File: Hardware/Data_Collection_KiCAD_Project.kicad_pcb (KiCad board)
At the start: 4 copper layers, 80 x 87.2 mm, 77 parts, among them IC1 STM32L562VET6Q, J1 USB_B_Micro, J2 Conn_Coaxial, J3 L717SDC37P1ACH4F, Q1 SI1040X-T1-GE3, U1 LM317T, U2 USBLC6-2SC6, U3 MCP9808_MSOP, U4 MAX-8Q, U6 W25Q32JVSS, U7 MS5607-02BA, U8 BNO055, U9 KX134-1211, Y1 32MHz, Y2 32.768kHz

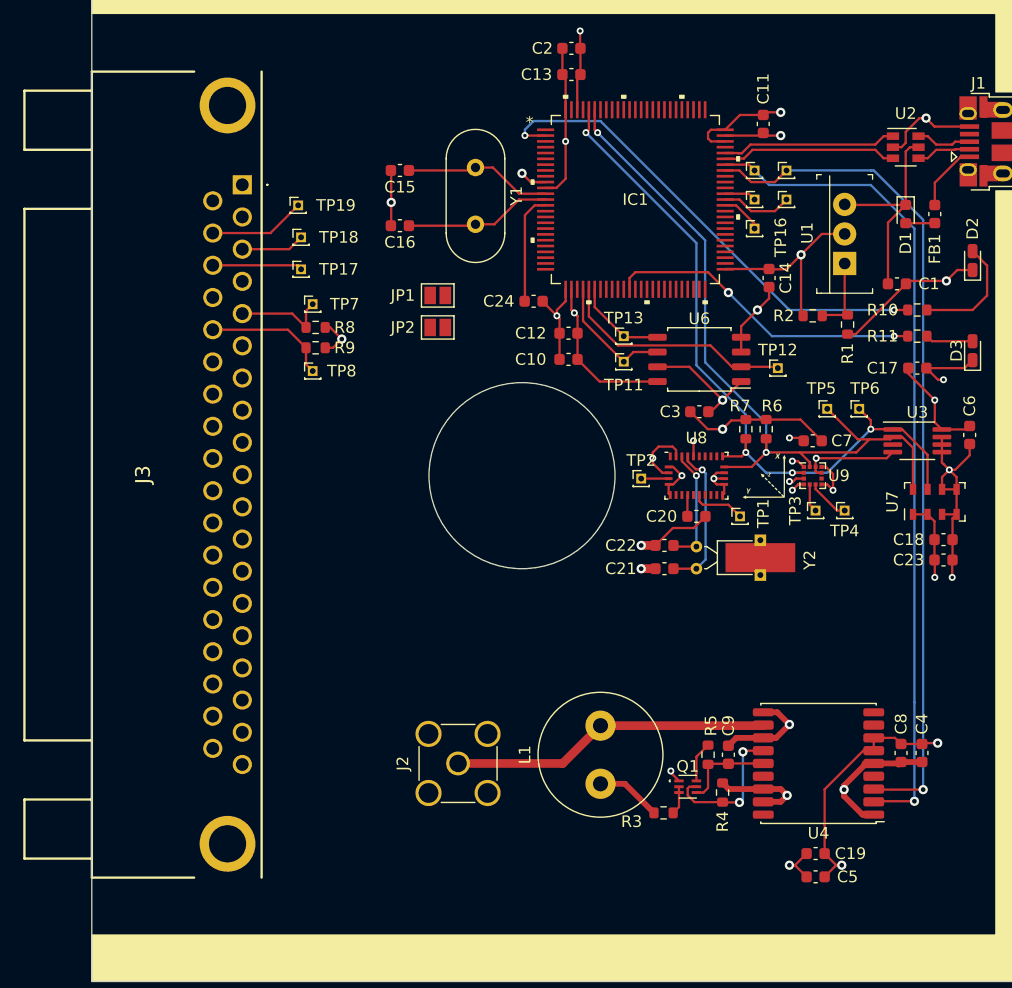
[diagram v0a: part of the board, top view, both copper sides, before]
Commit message: GPS layout change and test point tweaks
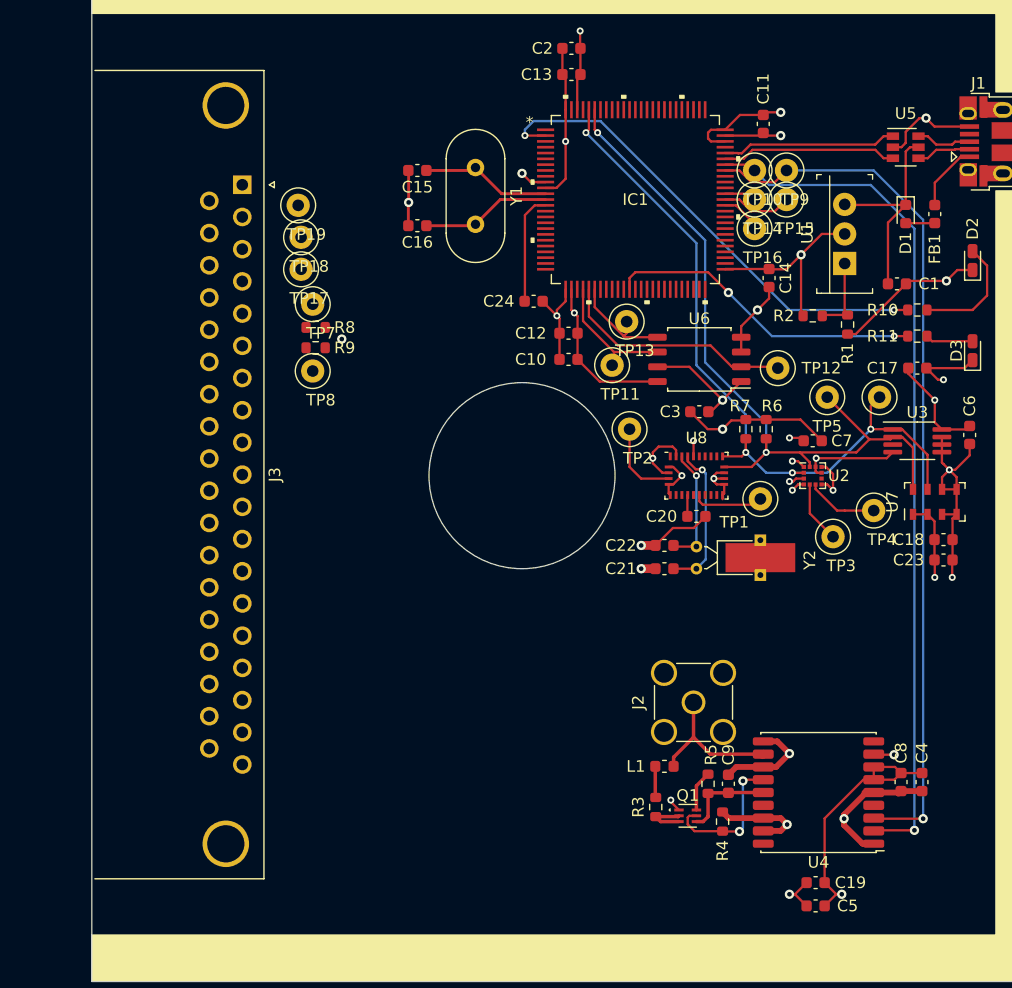
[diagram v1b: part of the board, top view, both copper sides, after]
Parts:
- removed G***: LOGO, XYZ:XYZ_Plane
- removed JP1: VDDA Bridge, Jumper:SolderJumper-2_P1.3mm_Open_Pad1.0x1.5mm
- removed JP2: VDD_SMPS, Jumper:SolderJumper-2_P1.3mm_Open_Pad1.0x1.5mm
- J3: footprint L717SDC37P1ACH4F:L717SDC37P1ACH4F -> Connector_Dsub:DSUB-37_Male_Horizontal_P2.77x2.84mm_EdgePinOffset9.90mm_Housed_MountingHolesOffset11.32mm
- L1: footprint Inductor_THT:L_Radial_D10.5mm_P5.00mm_Abacron_AISR-01 -> Inductor_SMD:L_0603_1608Metric
- TP1, TP10, TP11, TP12, TP13, TP14, TP15, TP16, TP17, TP18, TP19, TP2, TP3, TP4, TP5, TP6, TP7, TP8, TP9: footprint Connector_PinHeader_1.00mm:PinHeader_1x01_P1.00mm_Vertical -> TestPoint:TestPoint_Loop_D1.80mm_Drill1.0mm_Beaded
- moved J2 20.9 mm to (131.8, 121.0)
- moved L1 5.70 mm to (129.2, 126.5), turned to 0 degrees
- moved TP2 4.37 mm to (126.2, 97.5)
- moved TP3 2.70 mm to (143.8, 106.7)
- moved C19 2.50 mm to (142.2, 136.5)
- moved C4 2.50 mm to (151.4, 127.8)
- moved C5 2.50 mm to (142.2, 138.5)
- moved C8 2.50 mm to (149.6, 127.8)
- moved C9 2.50 mm to (134.8, 128.0)
- moved Q1 2.50 mm to (131.2, 130.7)
- moved R4 2.50 mm to (134.2, 131.2)
- moved R5 2.50 mm to (133.0, 128.0)
- moved TP4 2.50 mm to (147.2, 104.5)
- moved U4 2.50 mm to (142.5, 128.7)
- moved TP1 2.30 mm to (137.5, 103.5)
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- renumbered U9 to U2, U2 to U5
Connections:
- net /Main Bus/Fire renamed /37 Pin DSUB Bus/Fire
- net /Main Bus/Fire_redundant renamed /37 Pin DSUB Bus/Fire_redundant
- IC1 pad 21: Net-(IC1-Pad21) -> +3V3
- IC1 pad 46: Net-(IC1-Pad46) -> +3V3
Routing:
- net /MAX-8Q/GPS_ANT_NET: track 27.6 -> 12.9 mm
- net /EXT_SDA: track 10.9 -> 0.81 mm
- net /SPI2_MOSI: track 8.33 -> 0.00 mm
- net /EXT_SCL: track 8.21 -> 0.81 mm
- net /SPI2_SCK: track 7.74 -> 0.49 mm
- net /SPI2_MISO: track 5.48 -> 0.00 mm
- net /BNO055/~BNO055_BTL: track 2.36 -> 7.03 mm
- net Net-(L1-Pad1): track 6.56 -> 2.69 mm
- net /KX134-1211/KX134_INT1: track 2.44 -> 5.32 mm
- net /USART1_TX: track 72.9 -> 75.4 mm
- net /USART1_RX: track 71.3 -> 73.8 mm
- net /KX134-1211/KX134_INT2: track 3.65 -> 6.15 mm
- net Net-(Q1-Pad2): track 2.46 -> 4.21 mm
- net /BNO055/~BNO055_RESET: track 4.58 -> 6.12 mm
- net Net-(C15-Pad1): track 12.8 -> 11.3 mm
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
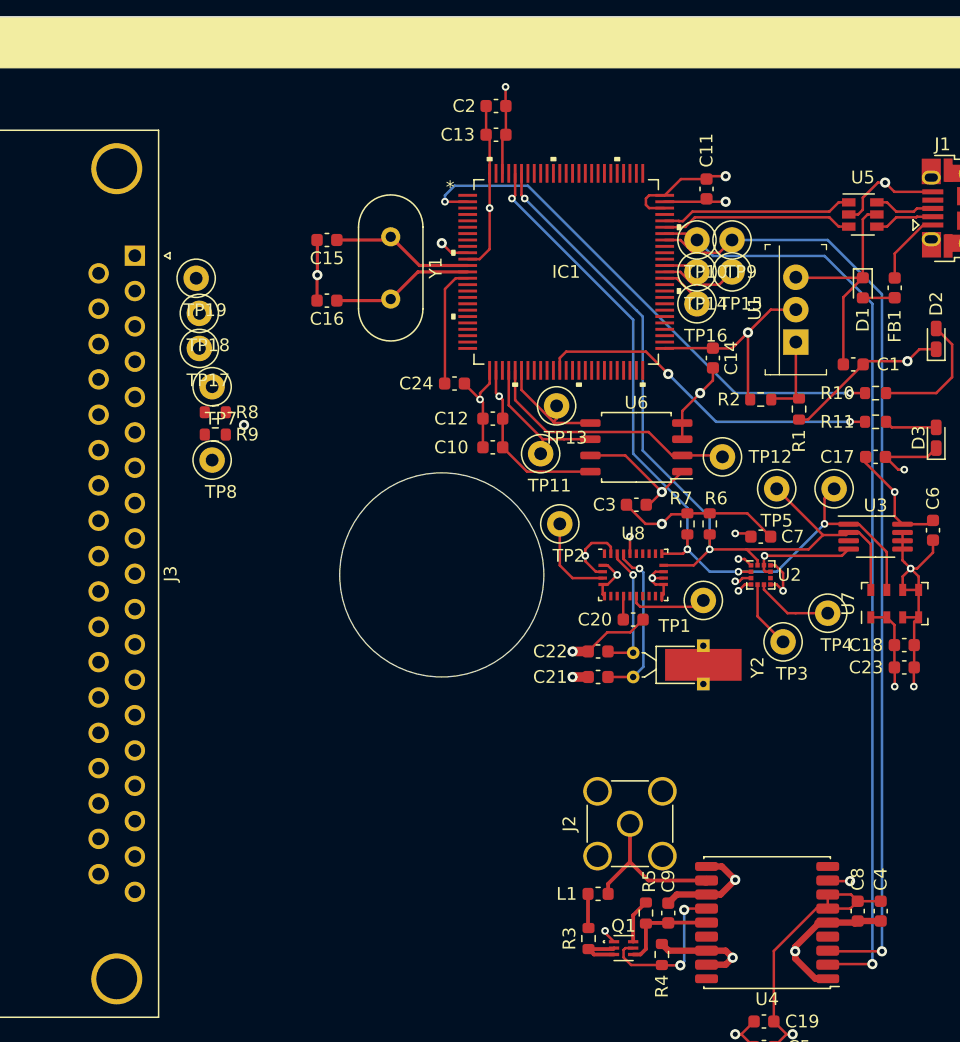
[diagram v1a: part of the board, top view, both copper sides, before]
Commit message: Finalized
Everything is routed. There are probably some things that need rerouting or adjustment.
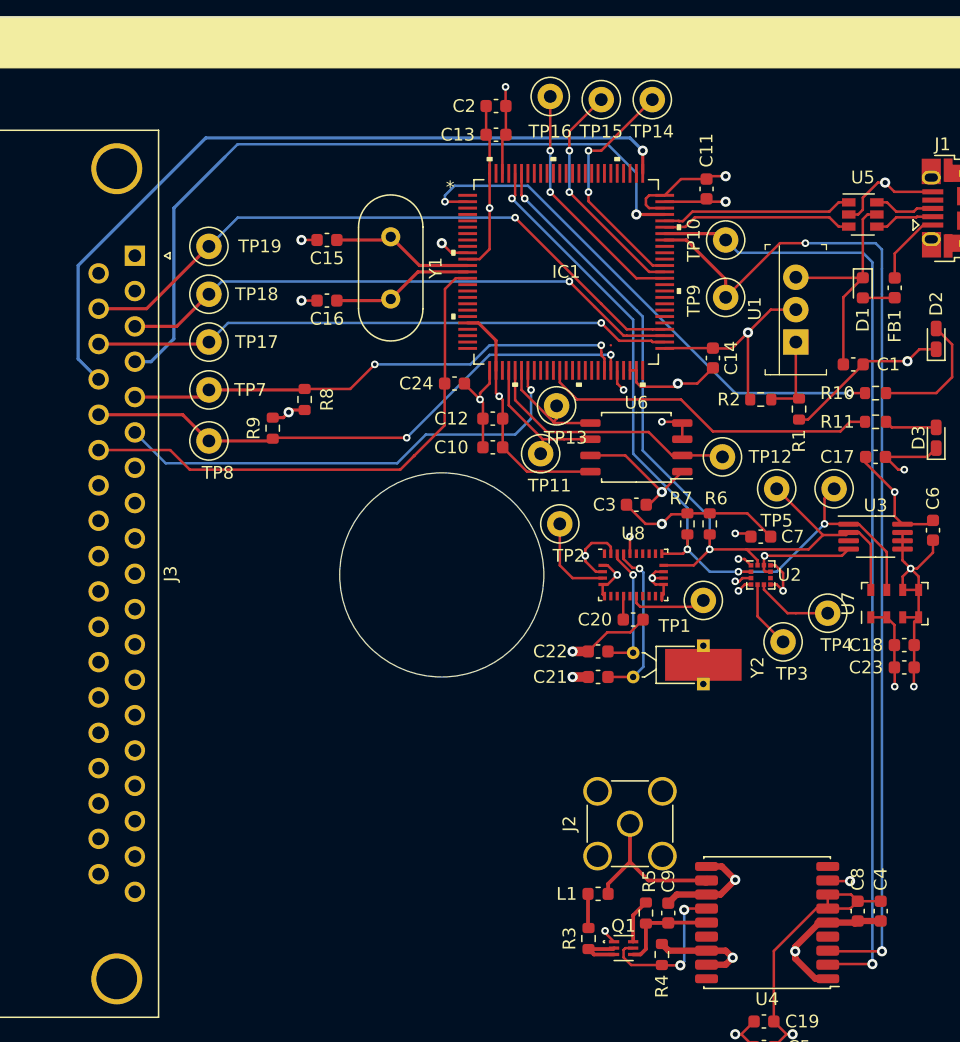
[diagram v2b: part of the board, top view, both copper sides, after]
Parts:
- moved TP16 19.9 mm to (125.5, 64.0)
- moved TP15 17.0 mm to (129.5, 64.2)
- moved TP14 13.9 mm to (133.5, 64.2)
- moved R8 7.07 mm to (106.2, 87.7), turned to 270 degrees
- moved R9 4.53 mm to (103.8, 90.0), turned to 90 degrees
- moved TP9 4.53 mm to (139.2, 79.7)
- moved TP19 2.69 mm to (98.8, 75.7)
- moved TP10 2.25 mm to (139.2, 75.2)
- moved TP18 1.68 mm to (98.8, 79.5)
- moved TP8 1.52 mm to (98.8, 91.0)
- moved TP17 0.90 mm to (98.8, 83.2)
- moved TP7 0.35 mm to (98.8, 87.0)
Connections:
- J3 pad 20: +5V -> Net-(J3-Pad20)
- J3 pad 37: +5V -> Net-(J3-Pad37)
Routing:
- net /SWCLK: track 0.00 -> 60.2 mm, vias 0 -> 1
- net /SWDIO: track 0.00 -> 58.8 mm, vias 0 -> 1
- net /SPI2_MOSI: track 0.00 -> 50.9 mm, vias 0 -> 1
- net /SPI2_MISO: track 0.00 -> 45.5 mm, vias 0 -> 1
- net /SPI2_SCK: track 0.49 -> 45.7 mm, vias 0 -> 1
- net /EXT_SDA: track 0.81 -> 45.0 mm, vias 0 -> 2
- net /EXT_SCL: track 0.81 -> 40.3 mm, vias 0 -> 2
- net /I2C_ALERT: track 0.00 -> 37.4 mm, vias 0 -> 1
- net /NRST: track 9.55 -> 42.2 mm
- net Net-(IC1-Pad64): track 2.74 -> 18.7 mm, vias 0 -> 2
- net Net-(IC1-Pad62): track 3.60 -> 19.3 mm, vias 0 -> 2
- net Net-(IC1-Pad63): track 6.11 -> 18.3 mm, vias 0 -> 2
- net +3V3: track 117.6 -> 126.8 mm, vias 13 -> 14
- net /USART1_TX: track 75.4 -> 81.0 mm, vias 1 -> 2
- net GND: track 157.6 -> 159.8 mm, vias 26 -> 28
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
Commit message: Schematic Tweaks and Board Dimensioned
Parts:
- removed TP10, TP11, TP12, TP13, TP17, TP18, TP19, TP5, TP6, TP7, TP8, TP9: Debug Pad, TestPoint:TestPoint_Loop_D1.80mm_Drill1.0mm_Beaded
- added J4: I2C1 Debug, Connector_PinHeader_2.54mm:PinHeader_1x02_P2.54mm_Vertical, F.Cu at (237.4, -162.9)
- added J5: EXT I2c Debug, Connector_PinHeader_2.54mm:PinHeader_1x02_P2.54mm_Vertical, F.Cu at (242.0, -162.9)
- added J6: UART Debug, Connector_PinHeader_2.54mm:PinHeader_1x02_P2.54mm_Vertical, F.Cu at (246.7, -162.9)
- added J7: SPI 1 Debug, Connector_PinHeader_2.54mm:PinHeader_1x03_P2.54mm_Vertical, F.Cu at (228.1, -162.9)
- added J8: Ext SPI Debug, Connector_PinHeader_2.54mm:PinHeader_1x03_P2.54mm_Vertical, F.Cu at (232.7, -162.9)
- added JP1: 5V Disconnect, Jumper:SolderJumper-2_P1.3mm_Bridged_Pad1.0x1.5mm, F.Cu at (227.9, -146.7)
- C1, C10, C11, C12, C13, C14, C15, C16, C17, C18, C19, C2, C20, C21, C22, C23, C24, C3, C4, C5, C6, C7, C8, C9, FB1: footprint Capacitor_SMD:C_0603_1608Metric -> Capacitor_SMD:C_0603_1608Metric_Pad1.08x0.95mm_HandSolder
- D1: footprint Diode_SMD:D_0603_1608Metric -> Diode_SMD:D_0603_1608Metric_Pad1.05x0.95mm_HandSolder
- D2, D3: footprint Diode_SMD:D_0603_1608Metric_Castellated -> Diode_SMD:D_0603_1608Metric_Pad1.05x0.95mm_HandSolder
- J1: value USB_B_Micro -> 10118192-0001LF; footprint Connector_USB:USB_Micro-B_Amphenol_10103594-0001LF_Horizontal -> Connector_USB:USB_Micro-B_Wuerth_614105150721_Vertical
- J3: footprint Connector_Dsub:DSUB-37_Male_Horizontal_P2.77x2.84mm_EdgePinOffset9.90mm_Housed_MountingHolesOffset11.32mm -> RDT_Custom_Footprints:L717SDC37P1ACH4F
- L1: footprint Inductor_SMD:L_0603_1608Metric -> Capacitor_SMD:C_0603_1608Metric_Pad1.08x0.95mm_HandSolder
- R1, R10, R11, R2, R3, R4, R5, R6, R7, R8, R9: footprint Resistor_SMD:R_0603_1608Metric -> Resistor_SMD:R_0603_1608Metric_Pad0.98x0.95mm_HandSolder
- moved C5 268.6 mm to (297.7, -80.5)
- moved C10 265.7 mm to (292.8, -111.3)
- moved C12 265.7 mm to (292.8, -113.5)
- moved C13 265.7 mm to (293.0, -135.8)
- moved C15 265.7 mm to (279.8, -127.5)
- moved C16 265.7 mm to (279.8, -122.8)
- moved C2 265.7 mm to (293.0, -138.0)
- moved C24 265.7 mm to (289.8, -116.3)
- moved R8 265.7 mm to (278.0, -115.0)
- moved R9 265.7 mm to (275.5, -112.8)
- moved Y1 265.7 mm to (284.8, -127.8)
- moved C1 261.8 mm to (331.5, -103.0)
- moved C11 261.8 mm to (320.0, -116.8)
- moved C14 261.8 mm to (320.5, -103.5)
- moved C17 261.8 mm to (333.2, -95.8)
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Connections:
- IC1 pad 1: Net-(IC1-Pad1) -> (no net)
- IC1 pad 15: Net-(IC1-Pad15) -> (no net)
- IC1 pad 16: Net-(IC1-Pad16) -> (no net)
- IC1 pad 17: Net-(IC1-Pad17) -> (no net)
- IC1 pad 18: Net-(IC1-Pad18) -> (no net)
- IC1 pad 19: Net-(IC1-Pad19) -> (no net)
- IC1 pad 20: Net-(IC1-Pad20) -> (no net)
- IC1 pad 22: Net-(IC1-Pad22) -> (no net)
- IC1 pad 23: Net-(IC1-Pad23) -> (no net)
- IC1 pad 24: Net-(IC1-Pad24) -> (no net)
- IC1 pad 25: Net-(IC1-Pad25) -> (no net)
- IC1 pad 28: Net-(IC1-Pad28) -> (no net)
- IC1 pad 3: Net-(IC1-Pad3) -> (no net)
- IC1 pad 33: Net-(IC1-Pad33) -> (no net)
- IC1 pad 34: Net-(IC1-Pad34) -> (no net)
- IC1 pad 35: Net-(IC1-Pad35) -> (no net)
- IC1 pad 36: Net-(IC1-Pad36) -> (no net)
- IC1 pad 38: Net-(IC1-Pad38) -> (no net)
- IC1 pad 39: Net-(IC1-Pad39) -> (no net)
- IC1 pad 4: Net-(IC1-Pad4) -> (no net)
- IC1 pad 40: Net-(IC1-Pad40) -> (no net)
- IC1 pad 41: Net-(IC1-Pad41) -> (no net)
- IC1 pad 42: Net-(IC1-Pad42) -> (no net)
- IC1 pad 43: Net-(IC1-Pad43) -> (no net)
- IC1 pad 47: Net-(IC1-Pad47) -> (no net)
- IC1 pad 5: Net-(IC1-Pad5) -> (no net)
- IC1 pad 50: Net-(IC1-Pad50) -> (no net)
- IC1 pad 55: Net-(IC1-Pad55) -> (no net)
- IC1 pad 56: Net-(IC1-Pad56) -> (no net)
- IC1 pad 57: Net-(IC1-Pad57) -> (no net)
- IC1 pad 58: Net-(IC1-Pad58) -> (no net)
- IC1 pad 59: Net-(IC1-Pad59) -> (no net)
- IC1 pad 6: Net-(IC1-Pad6) -> (no net)
- IC1 pad 60: Net-(IC1-Pad60) -> (no net)
- IC1 pad 61: Net-(IC1-Pad61) -> (no net)
- IC1 pad 65: Net-(IC1-Pad65) -> (no net)
- IC1 pad 66: Net-(IC1-Pad66) -> (no net)
- IC1 pad 67: Net-(IC1-Pad67) -> (no net)
- IC1 pad 7: Net-(IC1-Pad7) -> (no net)
- IC1 pad 77: Net-(IC1-Pad77) -> (no net)
- IC1 pad 78: Net-(IC1-Pad78) -> (no net)
- IC1 pad 79: Net-(IC1-Pad79) -> (no net)
- IC1 pad 8: Net-(IC1-Pad8) -> (no net)
- IC1 pad 80: Net-(IC1-Pad80) -> (no net)
- IC1 pad 81: Net-(IC1-Pad81) -> (no net)
- IC1 pad 82: Net-(IC1-Pad82) -> (no net)
- IC1 pad 83: Net-(IC1-Pad83) -> (no net)
- IC1 pad 84: Net-(IC1-Pad84) -> (no net)
- IC1 pad 85: Net-(IC1-Pad85) -> (no net)
- IC1 pad 86: Net-(IC1-Pad86) -> (no net)
- IC1 pad 87: Net-(IC1-Pad87) -> (no net)
- IC1 pad 88: Net-(IC1-Pad88) -> (no net)
- IC1 pad 89: Net-(IC1-Pad89) -> (no net)
- IC1 pad 9: Net-(IC1-Pad9) -> (no net)
- IC1 pad 90: Net-(IC1-Pad90) -> (no net)
- IC1 pad 91: Net-(IC1-Pad91) -> (no net)
- IC1 pad 92: Net-(IC1-Pad92) -> (no net)
- IC1 pad 93: Net-(IC1-Pad93) -> (no net)
- IC1 pad 94: Net-(IC1-Pad94) -> (no net)
- IC1 pad 97: Net-(IC1-Pad97) -> (no net)
- IC1 pad 99: Net-(IC1-Pad99) -> (no net)
- J1 pad 4: Net-(J1-Pad4) -> (no net)
- J1 pad 6: Net-(J1-Pad6) -> (no net)
- J3 pad 10: Net-(J3-Pad10) -> (no net)
- J3 pad 11: Net-(J3-Pad11) -> (no net)
- J3 pad 12: Net-(J3-Pad12) -> (no net)
- J3 pad 13: Net-(J3-Pad13) -> (no net)
- J3 pad 14: Net-(J3-Pad14) -> (no net)
- J3 pad 15: Net-(J3-Pad15) -> (no net)
- J3 pad 16: Net-(J3-Pad16) -> (no net)
- J3 pad 17: Net-(J3-Pad17) -> (no net)
- J3 pad 20: Net-(J3-Pad20) -> /37 Pin DSUB Bus/Dsub_5v
- J3 pad 26: /37 Pin DSUB Bus/Fire_redundant -> (no net)
- J3 pad 27: Net-(J3-Pad27) -> (no net)
- J3 pad 28: Net-(J3-Pad28) -> (no net)
- J3 pad 29: Net-(J3-Pad29) -> (no net)
- J3 pad 30: Net-(J3-Pad30) -> (no net)
- J3 pad 31: Net-(J3-Pad31) -> (no net)
- J3 pad 32: Net-(J3-Pad32) -> (no net)
- J3 pad 33: Net-(J3-Pad33) -> (no net)
- J3 pad 34: Net-(J3-Pad34) -> (no net)
- J3 pad 35: Net-(J3-Pad35) -> (no net)
- J3 pad 36: Net-(J3-Pad36) -> (no net)
- J3 pad 37: Net-(J3-Pad37) -> /37 Pin DSUB Bus/Dsub_5v
- J3 pad 7: /37 Pin DSUB Bus/Fire -> (no net)
- J3 pad 8: Net-(J3-Pad8) -> (no net)
- J3 pad 9: Net-(J3-Pad9) -> (no net)
- U3 pad 3: /MCP9808/ALERT -> (no net)
- U4 pad 15: Net-(U4-Pad15) -> (no net)
- U4 pad 18: Net-(U4-Pad18) -> (no net)
- U4 pad 4: Net-(U4-Pad4) -> (no net)
- U4 pad 9: /MAX-8Q/~RESET -> (no net)
- U8 pad 1: Net-(U8-Pad1) -> (no net)
- U8 pad 10: /BNO055/BNO055_BTL_IND -> (no net)
- U8 pad 12: Net-(U8-Pad12) -> (no net)
- U8 pad 13: Net-(U8-Pad13) -> (no net)
- U8 pad 14: /BNO055/BNO055_INT -> (no net)
- U8 pad 21: Net-(U8-Pad21) -> (no net)
- U8 pad 22: Net-(U8-Pad22) -> (no net)
- U8 pad 23: Net-(U8-Pad23) -> (no net)
- U8 pad 24: Net-(U8-Pad24) -> (no net)
- U8 pad 7: Net-(U8-Pad7) -> (no net)
- U8 pad 8: Net-(U8-Pad8) -> (no net)
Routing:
- net GND: track 159.8 -> 0.00 mm, vias 28 -> 0
- net +3V3: track 126.8 -> 0.00 mm, vias 14 -> 0
- net /USART1_TX: track 81.0 -> 0.00 mm, vias 2 -> 0
- net /USART1_RX: track 75.7 -> 0.00 mm, vias 1 -> 0
- net /I2C1_SCL: track 64.7 -> 0.00 mm, vias 2 -> 0
- net /I2C1_SDA: track 64.4 -> 0.00 mm, vias 4 -> 0
- net /SWCLK: track 60.2 -> 0.00 mm, vias 1 -> 0
- net /SWDIO: track 58.8 -> 0.00 mm, vias 1 -> 0
- net /SPI2_MOSI: track 50.9 -> 0.00 mm, vias 1 -> 0
- net /SPI2_SCK: track 45.7 -> 0.00 mm, vias 1 -> 0
- net /SPI2_MISO: track 45.5 -> 0.00 mm, vias 1 -> 0
- net /EXT_SDA: track 45.0 -> 0.00 mm, vias 2 -> 0
- net Net-(IC1-Pad2): track 42.2 -> 0.00 mm, vias 2 -> 0
- net /NRST: track 42.2 -> 0.00 mm
- net /EXT_SCL: track 40.3 -> 0.00 mm, vias 2 -> 0
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- removed copper zone on In2.Cu, net +3V3
- removed copper zone on In1.Cu, net GND
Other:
- board size 80 x 87.2 mm -> 80 x 93.2 mm
- net class DIFF_90_USB added: clearance 0.2, trace_width 0.175006, via_dia 0.4, via_drill 0.2
- net class Default: clearance 0.15 -> 0.05; trace_width 0.2 -> 0.25
- rule pad_to_mask_clearance: 0 -> 0.051
- rule trace_clearance: 0.15 -> 0.05
- rule trace_min: 0.2 -> 0.09
- rule via_min_drill: 0.3 -> 0.2

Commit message: routing progress and pin reassignment
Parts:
- removed TP4: Debug Pad, TestPoint:TestPoint_Loop_D1.80mm_Drill1.0mm_Beaded
- TP1, TP14, TP15, TP16, TP2, TP3: footprint TestPoint:TestPoint_Loop_D1.80mm_Drill1.0mm_Beaded -> TestPoint:TestPoint_Pad_D1.0mm
- moved C13 285.0 mm to (128.6, 97.1), turned to 135 degrees
- moved U5 277.5 mm to (136.2, 81.6)
- moved C14 272.0 mm to (140.2, 100.2), turned to 315 degrees
- moved J1 267.9 mm to (143.8, 79.7), turned to 135 degrees
- moved C23 267.0 mm to (139.0, 101.5), turned to 135 degrees
- moved TP2 264.3 mm to (128.6, 103.1)
- moved TP1 262.5 mm to (135.3, 102.3)
- moved C20 259.9 mm to (132.0, 102.2), turned to 0 degrees
- moved Y1 258.7 mm to (113.2, 66.0), turned to 225 degrees
- moved U2 258.6 mm to (143.5, 98.5)
- moved U8 258.6 mm to (133.5, 98.5)
- moved TP3 257.9 mm to (143.6, 101.1)
- moved C16 256.0 mm to (107.1, 66.3), turned to 45 degrees
- moved C15 255.0 mm to (110.4, 63.1), turned to 225 degrees
- moved C22 253.2 mm to (128.6, 94.6), turned to 135 degrees
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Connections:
- IC1 pad 29: /SPI1_SCK -> /SPI2_SCK
- IC1 pad 30: /SPI1_MISO -> /SPI2_MISO
- IC1 pad 31: /SPI1_MOSI -> /SPI2_MOSI
- IC1 pad 52: /SPI2_SCK -> (no net)
- IC1 pad 53: /SPI2_MISO -> (no net)
- IC1 pad 54: /SPI2_MOSI -> (no net)
- IC1 pad 59: (no net) -> /I2C1_SCL
- IC1 pad 60: (no net) -> /I2C1_SDA
- IC1 pad 78: (no net) -> /SPI1_SCK
- IC1 pad 79: (no net) -> /SPI1_MISO
- IC1 pad 80: (no net) -> /SPI1_MOSI
- IC1 pad 95: /I2C1_SCL -> (no net)
- IC1 pad 96: /I2C1_SDA -> (no net)
- J3 pad MH1: (no net) -> GND
- J3 pad MH2: (no net) -> GND
- U2 pad 6: /KX134-1211/KX134_INT2 -> (no net)
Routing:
- net GND: track 0.00 -> 60.4 mm, vias 0 -> 5
- net +3V3: track 0.00 -> 20.2 mm, vias 0 -> 4
- net /USB Connector and ESD/USB_CONN_D-: track 0.00 -> 10.6 mm
- net /SPI1_MISO: track 0.00 -> 10.5 mm, vias 0 -> 2
- net /I2C1_SCL: track 0.00 -> 10.4 mm
- net Net-(C16-Pad1): track 0.00 -> 9.98 mm
- net Net-(C15-Pad1): track 0.00 -> 9.89 mm
- net /USB Connector and ESD/USB_CONN_D+: track 0.00 -> 8.77 mm
- net /SPI1_SCK: track 0.00 -> 8.63 mm
- net /USB_D-: track 0.00 -> 8.21 mm
- net /USB_D+: track 0.00 -> 7.98 mm
- net /I2C1_SDA: track 0.00 -> 7.94 mm, vias 0 -> 2
- net Net-(C22-Pad2): track 0.00 -> 6.65 mm
- net /BNO055/~BNO055_BTL: track 0.00 -> 5.94 mm
- net /SPI1_MOSI: track 0.00 -> 5.85 mm
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- added copper zone on 3.3V.Cu, net +3V3
- added copper zone on GND.Cu, net GND
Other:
- net class DIFF_90_USB: clearance 0.2 -> 0.05

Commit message: Routing Progress
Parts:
- moved L1 115.7 mm to (110.3, 122.0)
- moved R3 115.7 mm to (109.6, 125.5)
- moved R4 115.7 mm to (115.3, 126.7)
- moved U4 110.2 mm to (127.2, 118.8), turned to 315 degrees
- moved U3 102.4 mm to (145.4, 90.9), turned to 45 degrees
- moved C9 100.6 mm to (134.2, 126.2), turned to 225 degrees
- moved U7 98.8 mm to (151.3, 97.0)
- moved R5 98.7 mm to (135.5, 127.5), turned to 45 degrees
- moved C18 98.7 mm to (151.9, 99.7)
- moved Q1 95.4 mm to (137.5, 130.0), turned to 135 degrees
- moved R6 94.2 mm to (141.0, 88.7), turned to 45 degrees
- moved R7 91.8 mm to (140.8, 86.5), turned to 45 degrees
- moved R1 87.3 mm to (149.0, 65.0), turned to 135 degrees
- moved J2 84.7 mm to (152.2, 121.5)
- moved C2 81.6 mm to (151.5, 65.0), turned to 135 degrees
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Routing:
- net /I2C1_SDA: track 7.94 -> 52.6 mm, vias 2 -> 4
- net /I2C1_SCL: track 10.4 -> 47.8 mm, vias 0 -> 2
- net +3V3: track 20.2 -> 55.4 mm
- net +5V: track 0.00 -> 29.4 mm
- net GND: track 60.4 -> 84.9 mm, vias 5 -> 7
- net Net-(FB1-Pad2): track 0.00 -> 5.63 mm, vias 0 -> 1
- net Net-(R1-Pad1): track 0.00 -> 5.48 mm
- net Net-(D1-Pad2): track 0.00 -> 1.77 mm
